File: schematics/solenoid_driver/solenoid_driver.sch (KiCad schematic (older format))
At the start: 11 parts

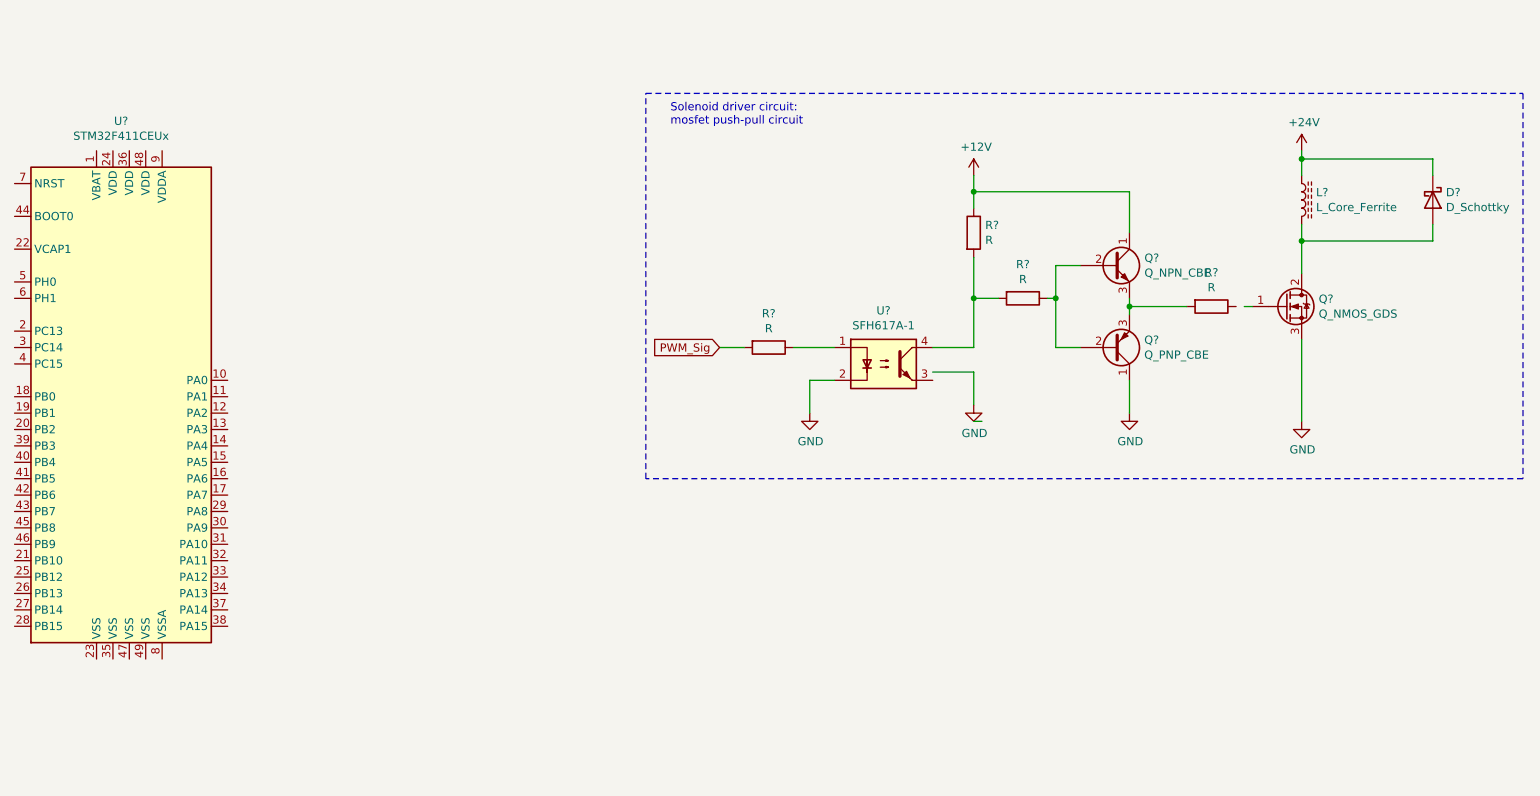
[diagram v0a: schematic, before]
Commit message: updated schematics: put driver circuit in hierachical sheet
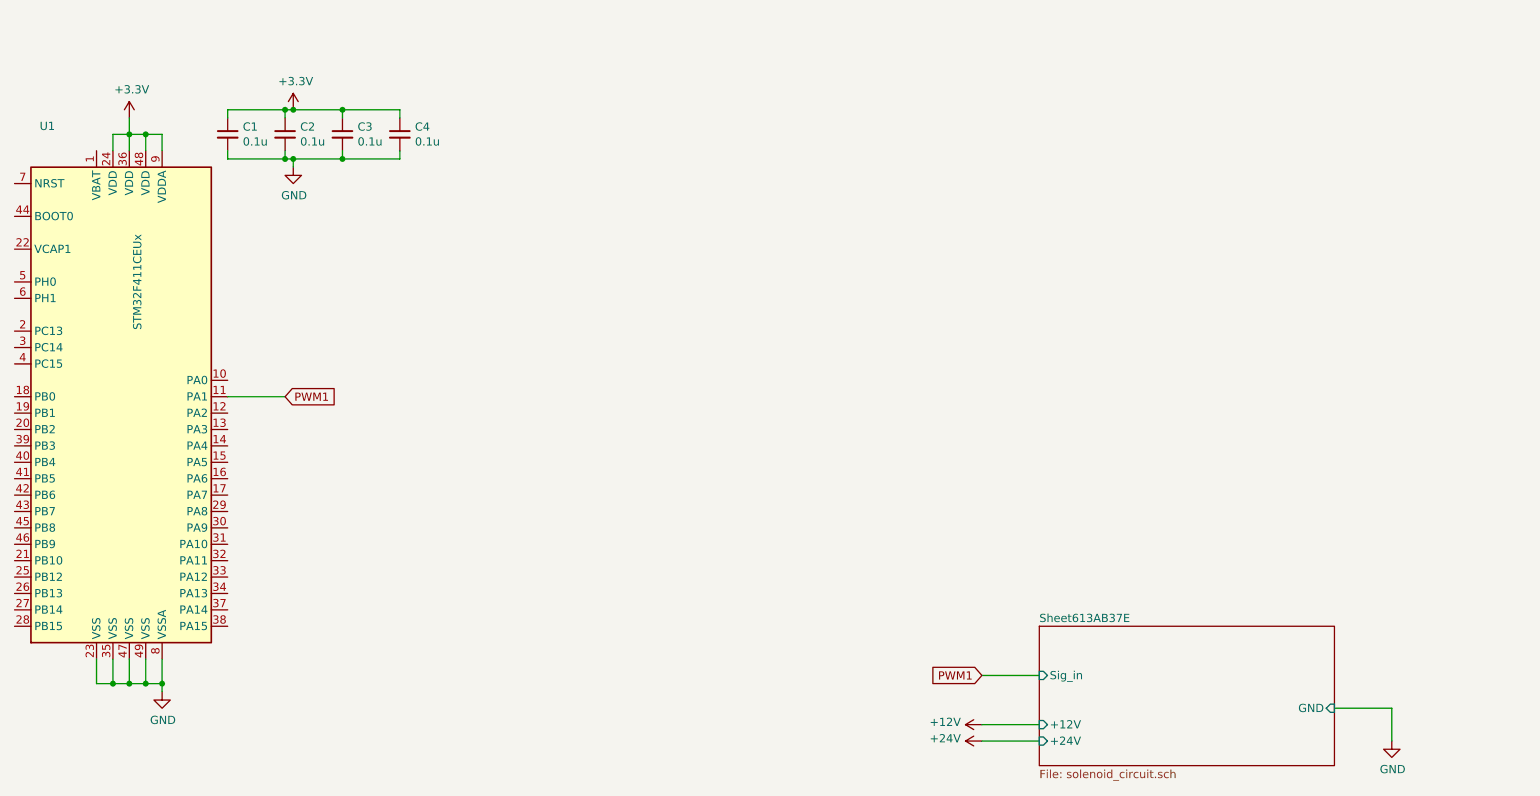
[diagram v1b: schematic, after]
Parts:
- removed D?: D_Schottky, symbol Device:D_Schottky
- removed L?: L_Core_Ferrite, symbol Device:L_Core_Ferrite
- removed Q?: Q_NPN_CBE, symbol Device:Q_NPN_CBE
- removed Q?: Q_PNP_CBE, symbol Device:Q_PNP_CBE
- removed Q?: Q_NMOS_GDS, symbol Device:Q_NMOS_GDS
- removed R? (x4): R, symbol Device:R
- removed U?: SFH617A-1, Package_DIP:DIP-4_W7.62mm, symbol Isolator:SFH617A-1
- added C1, C2, C3, C4: 0.1u, symbol Device:C_Small
- gave numbers to parts that had none: 1
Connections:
- net labels added: +3.3V, PWM1
- net labels removed: PWM_Sig
- wire segments 34 -> 41
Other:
- note removed: "Solenoid driver circuit: \nmosfet push-pull circuit"

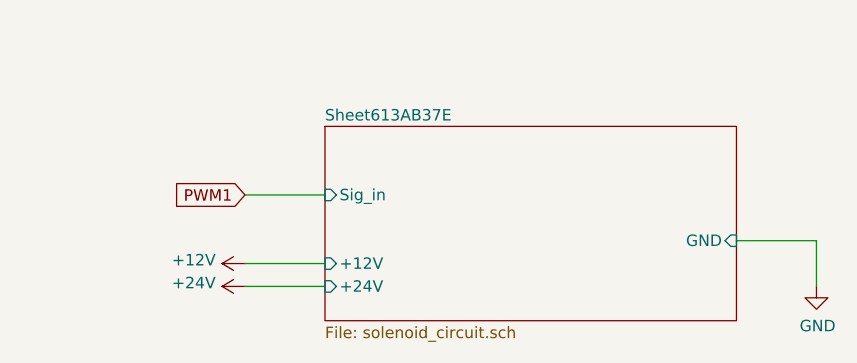
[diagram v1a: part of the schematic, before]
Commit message: created mtrix_controller project, updated schematic on solenoid_driver
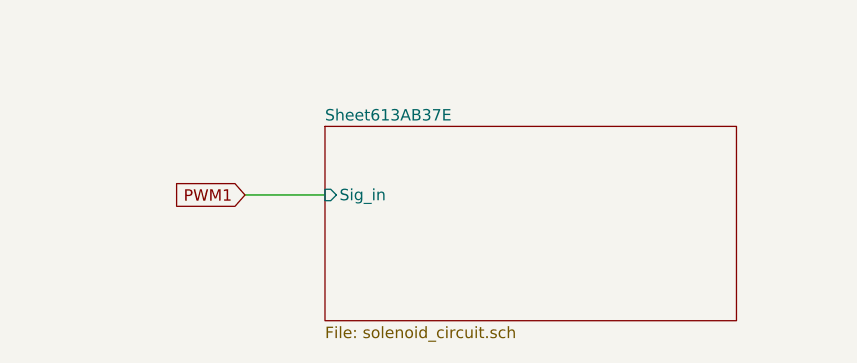
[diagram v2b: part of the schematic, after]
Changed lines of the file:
@@
 F1 "solenoid_circuit.sch" 50
 F2 "Sig_in" I L 8100 5150 50
-F3 "+12V" I L 8100 5450 50
-F4 "+24V" I L 8100 5550 50
-F5 "GND" I R 9900 5350 50
 $EndSheet
 Wire Wire Line
@@
 Text GLabel 7750 5150 0    50   Input ~ 0
 PWM1
-$Comp
-L power:GND #PWR07
-U 1 1 613B6B06
-P 10250 5550
-F 0 "#PWR07" H 10250 5300 50  0001 C CNN
-F 1 "GND" H 10255 5377 50  0000 C CNN
-F 2 "" H 10250 5550 50  0001 C CNN
-F 3 "" H 10250 5550 50  0001 C CNN
-	1    10250 5550
-	1    0    0    -1
-$EndComp
-Wire Wire Line
-	10250 5550 10250 5350
-Wire Wire Line
-	10250 5350 9900 5350
-$Comp
-L power:+12V #PWR05
-U 1 1 613B71E0
-P 7750 5450
-F 0 "#PWR05" H 7750 5300 50  0001 C CNN
-F 1 "+12V" V 7765 5578 50  0000 L CNN
-F 2 "" H 7750 5450 50  0001 C CNN
-F 3 "" H 7750 5450 50  0001 C CNN
-	1    7750 5450
-	0    -1   -1   0
-$EndComp
-$Comp
-L power:+24V #PWR06
-U 1 1 613B76A1
-P 7750 5550
-F 0 "#PWR06" H 7750 5400 50  0001 C CNN
-F 1 "+24V" V 7765 5678 50  0000 L CNN
-F 2 "" H 7750 5550 50  0001 C CNN
-F 3 "" H 7750 5550 50  0001 C CNN
-	1    7750 5550
-	0    -1   -1   0
-$EndComp
-Wire Wire Line
-	7750 5550 8100 5550
-Wire Wire Line
-	7750 5450 8100 5450
 Text GLabel 3500 3450 2    50   Input ~ 0
 PWM1

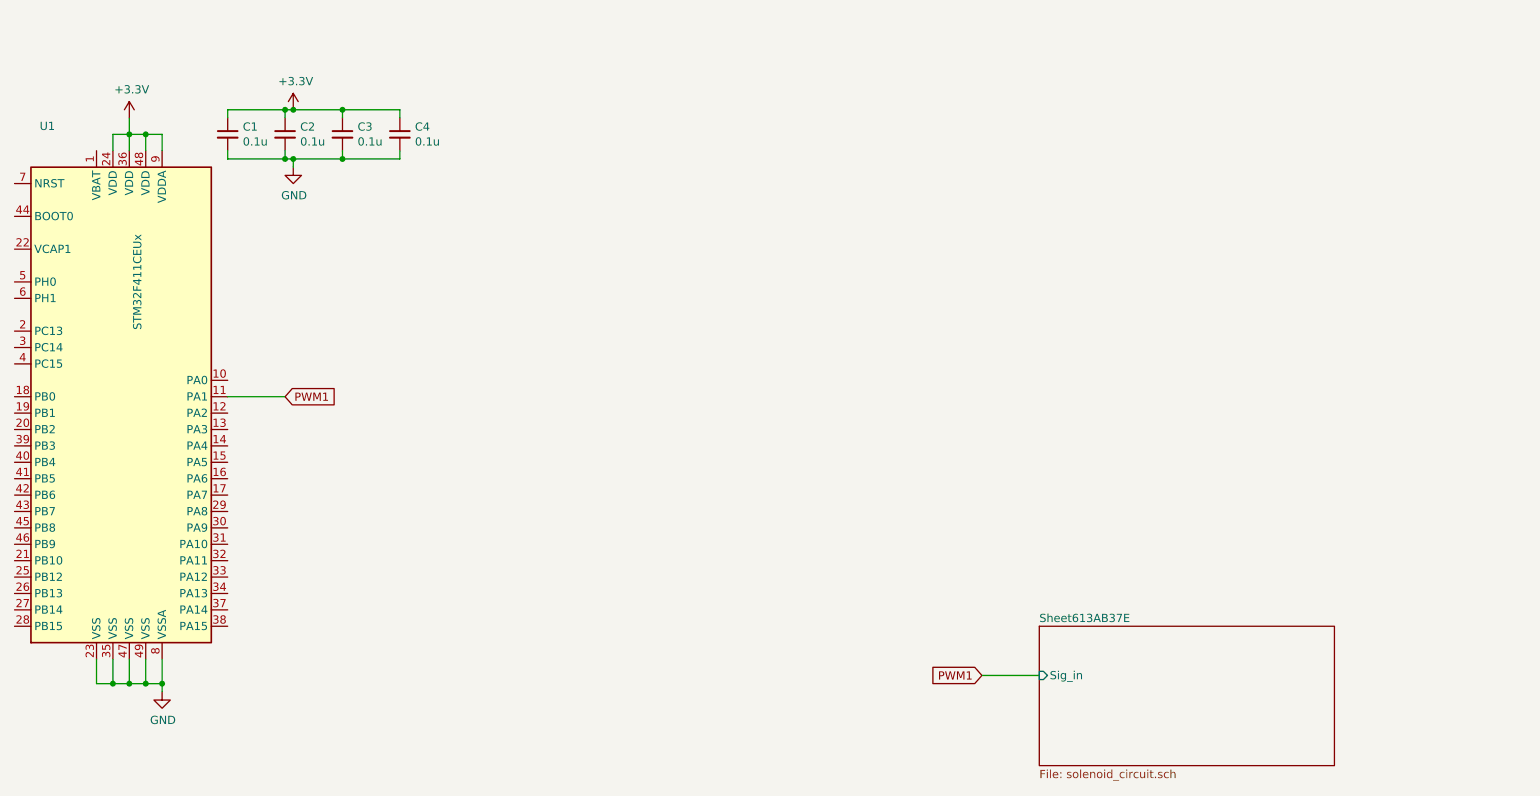
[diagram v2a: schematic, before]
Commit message: updated schematics to add a op amp for current sensing
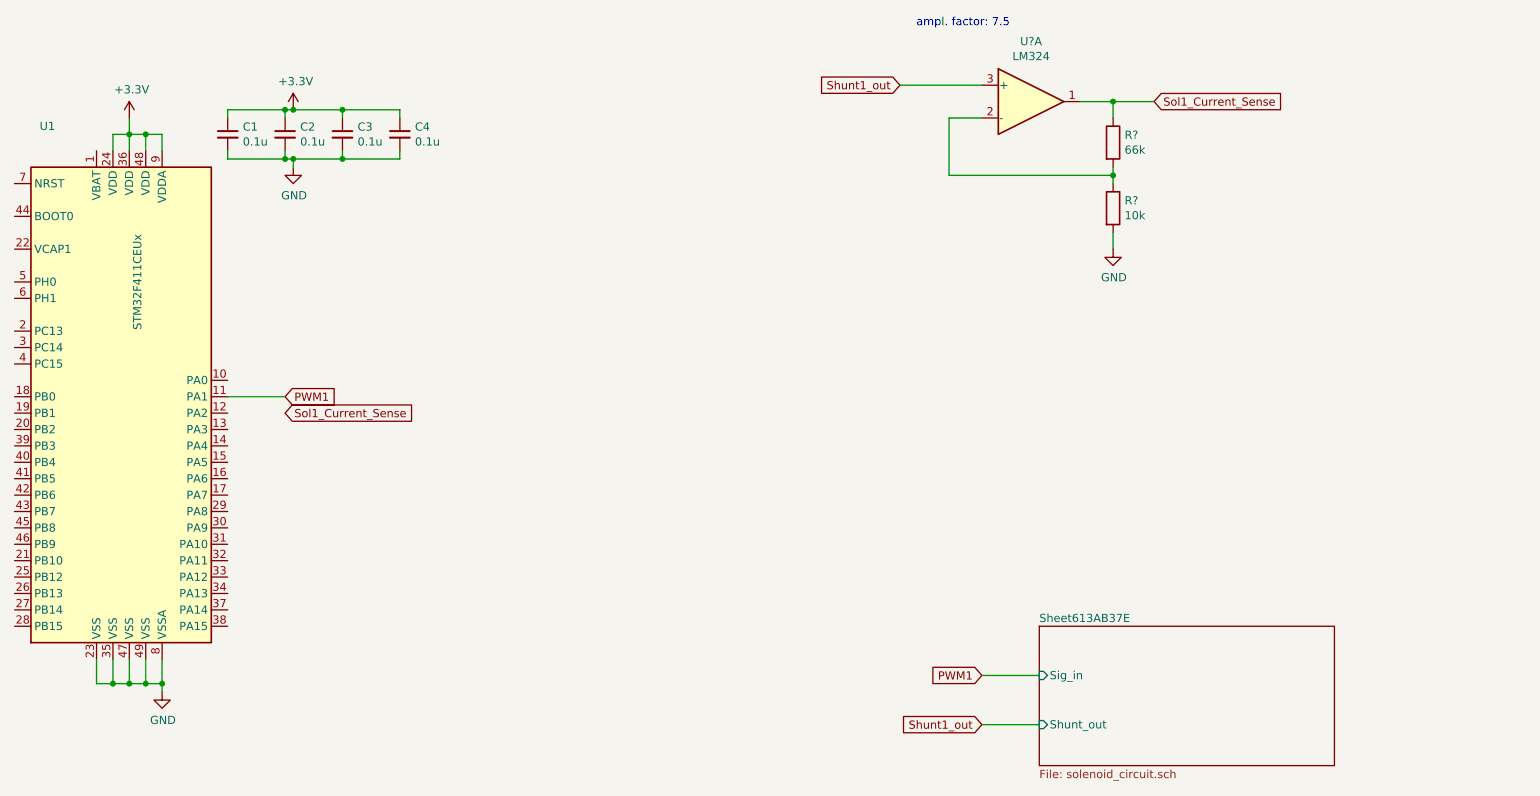
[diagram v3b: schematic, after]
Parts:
- added R?: 66k, symbol Device:R
- added R?: 10k, symbol Device:R
- added U?: LM324, symbol Amplifier_Operational:LM324
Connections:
- net GND: now also R?.2
- new net: R?.1, R?.2, U?.2 (-)
- new net Shunt1_out: U?.3 (+)
- new net Sol1_Current_Sense: R?.1, U?.1
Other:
- note added: "ampl. factor: 7.5"
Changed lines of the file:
@@
 F1 "solenoid_circuit.sch" 50
 F2 "Sig_in" I L 8100 5150 50
+F3 "Shunt_out" I L 8100 5450 50
 $EndSheet
 Wire Wire Line
@@
 Wire Wire Line
 	3550 2000 3850 2000
+$Comp
+L Amplifier_Operational:LM324 U?
+U 1 1 616CD86C
+P 8050 1650
+F 0 "U?" H 8050 2017 50  0000 C CNN
+F 1 "LM324" H 8050 1926 50  0000 C CNN
+F 2 "" H 8000 1750 50  0001 C CNN
+F 3 "http://www.ti.com/lit/ds/symlink/lm2902-n.pdf" H 8100 1850 50  0001 C CNN
+	1    8050 1650
+	1    0    0    -1
+$EndComp
+Text GLabel 7750 5450 0    50   Input ~ 0
+Shunt1_out
+Wire Wire Line
+	7750 5450 8100 5450
+Text GLabel 7250 1550 0    50   Input ~ 0
+Shunt1_out
+Wire Wire Line
+	7250 1550 7750 1550
+$Comp
+L Device:R R?
+U 1 1 616D0DDE
+P 8550 1900
+F 0 "R?" H 8620 1946 50  0000 L CNN
+F 1 "66k" H 8620 1855 50  0000 L CNN
+F 2 "" V 8480 1900 50  0001 C CNN
+F 3 "~" H 8550 1900 50  0001 C CNN
+	1    8550 1900
+	1    0    0    -1
+$EndComp
+$Comp
+L Device:R R?
+U 1 1 616D1600
+P 8550 2300
+F 0 "R?" H 8620 2346 50  0000 L CNN
+F 1 "10k" H 8620 2255 50  0000 L CNN
+F 2 "" V 8480 2300 50  0001 C CNN
+F 3 "~" H 8550 2300 50  0001 C CNN
+	1    8550 2300
+	1    0    0    -1
+$EndComp
+$Comp
+L power:GND #PWR?
+U 1 1 616D1B4E
+P 8550 2550
+F 0 "#PWR?" H 8550 2300 50  0001 C CNN
+F 1 "GND" H 8555 2377 50  0000 C CNN
+F 2 "" H 8550 2550 50  0001 C CNN
+F 3 "" H 8550 2550 50  0001 C CNN
+	1    8550 2550
+	1    0    0    -1
+$EndComp
+Wire Wire Line
+	8550 2550 8550 2450
+Wire Wire Line
+	8550 2150 8550 2100
+Wire Wire Line
+	8550 1750 8550 1650
+Wire Wire Line
+	8550 1650 8350 1650
+Wire Wire Line
+	7750 1750 7550 1750
+Wire Wire Line
+	7550 1750 7550 2100
+Wire Wire Line
+	7550 2100 8550 2100
+Connection ~ 8550 2100
+Wire Wire Line
+	8550 2100 8550 2050
+Text GLabel 8800 1650 2    50   Input ~ 0
+Sol1_Current_Sense
+Wire Wire Line
+	8800 1650 8550 1650
+Connection ~ 8550 1650
+Text Notes 7350 1200 0    50   ~ 0
+ampl. factor: 7.5
+Text GLabel 3500 3550 2    50   Input ~ 0
+Sol1_Current_Sense
 $EndSCHEMATC
